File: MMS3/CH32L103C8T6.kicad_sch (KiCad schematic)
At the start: 21 parts, among them J3 WCH Link, U2 CH32L103C8T6_C22398291, X3 X322525MOB4SI, X4 Q13FC1350000400

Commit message: kinda finished schematic
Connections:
- net +3.3V: no longer C30.1, C31.1, C32.1, C33.1, C34.1, R8.2, S1.2 (B), U2.1 (VBAT), U2.24 (VDD), U2.36 (VDD), U2.48 (VDD), U2.9 (VDDA)
- new net +3V3: C30.1, C31.1, C32.1, C33.1, C34.1, R8.2, S1.2 (B), U2.1 (VBAT), U2.24 (VDD), U2.36 (VDD), U2.48 (VDD), U2.9 (VDDA)
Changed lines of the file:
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@@
-	)
-	(symbol
-		(lib_id "power:+3.3V")
-		(at 187.96 120.65 0)
-		(unit 1)
-		(body_style 1)
-		(exclude_from_sim no)
-		(in_bom yes)
-		(on_board yes)
-		(in_pos_files yes)
-		(dnp no)
-		(fields_autoplaced yes)
-		(property "Reference" "#PWR016"
-			(at 187.96 124.46 0)
-			(hide yes)
-			(show_name no)
-			(do_not_autoplace no)
-			(effects
-				(font
-					(size 1.27 1.27)
-				)
-			)
-		)
-		(property "Value" "+3.3V"
-			(at 187.96 115.57 0)
-			(show_name no)
-			(do_not_autoplace no)
-			(effects
-				(font
-					(size 1.27 1.27)
-				)
-			)
-		)
-		(property "Footprint" ""
-			(at 187.96 120.65 0)
-			(hide yes)
-			(show_name no)
-			(do_not_autoplace no)
-			(effects
-				(font
-					(size 1.27 1.27)
-				)
-			)
-		)
-		(property "Datasheet" ""
-			(at 187.96 120.65 0)
-			(hide yes)
-			(show_name no)
-			(do_not_autoplace no)
-			(effects
-				(font
-					(size 1.27 1.27)
-				)
-			)
-		)
-		(property "Description" "Power symbol creates a global label with name \"+3.3V\""
-			(at 187.96 120.65 0)
-			(hide yes)
-			(show_name no)
-			(do_not_autoplace no)
-			(effects
-				(font
-					(size 1.27 1.27)
-				)
-			)
-		)
-		(pin "1"
-		)
-		(instances
-			(project "MMS3"
-				(path "/712cea22-140d-4c92-923f-f4998caf3ecd/ec639d08-3c03-4054-a7c4-c3d480e6d770/8d009271-d3bb-4150-9191-494f39201dbc"
-					(reference "#PWR016")
-					(unit 1)
-				)
-			)
-		)
 	)
 	(symbol
@@
 					(unit 1)
 				)
+			)
+		)
+	)
+	(symbol
+		(lib_id "power:+3V3")
+		(at 187.96 120.65 0)
+		(unit 1)
+		(body_style 1)
+		(exclude_from_sim no)
+		(in_bom yes)
+		(on_board yes)
+		(in_pos_files yes)
+		(dnp no)
+		(fields_autoplaced yes)
+		(property "Reference" "#PWR063"
+			(at 187.96 124.46 0)
+			(hide yes)
+			(show_name no)
+			(do_not_autoplace no)
+			(effects
+				(font
+					(size 1.27 1.27)
+				)
+			)
+		)
+		(property "Value" "+3V3"
+			(at 187.96 115.57 0)
+			(show_name no)
+			(do_not_autoplace no)
+			(effects
+				(font
+					(size 1.27 1.27)
+				)
+			)
+		)
+		(property "Footprint" ""
+			(at 187.96 120.65 0)
+			(hide yes)
+			(show_name no)
+			(do_not_autoplace no)
+			(effects
+				(font
+					(size 1.27 1.27)
+				)
+			)
+		)
+		(property "Datasheet" ""
+			(at 187.96 120.65 0)
+			(hide yes)
+			(show_name no)
+			(do_not_autoplace no)
+			(effects
+				(font
+					(size 1.27 1.27)
+				)
+			)
+		)
+		(property "Description" "Power symbol creates a global label with name \"+3V3\""
+			(at 187.96 120.65 0)
+			(hide yes)
+			(show_name no)
+			(do_not_autoplace no)
+			(effects
+				(font
+					(size 1.27 1.27)
+				)
+			)
+		)
+		(pin "1"
+		)
+		(instances
+			(project "MMS3"
+				(path "/712cea22-140d-4c92-923f-f4998caf3ecd/ec639d08-3c03-4054-a7c4-c3d480e6d770/8d009271-d3bb-4150-9191-494f39201dbc"
+					(reference "#PWR063")
+					(unit 1)
+				)

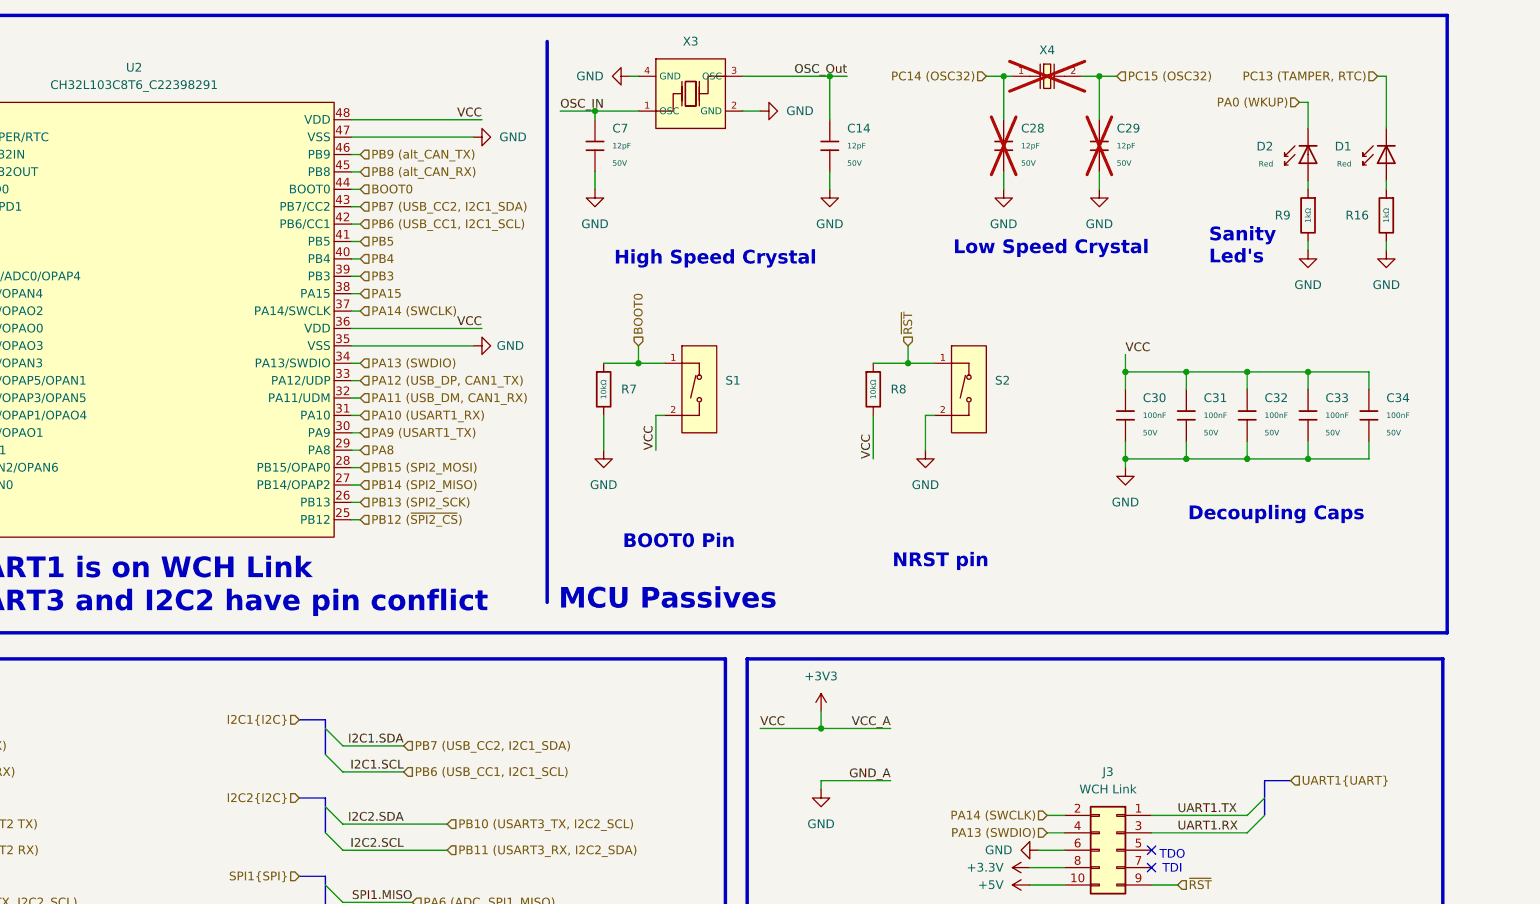
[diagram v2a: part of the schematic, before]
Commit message: updated schematic, removed annotation
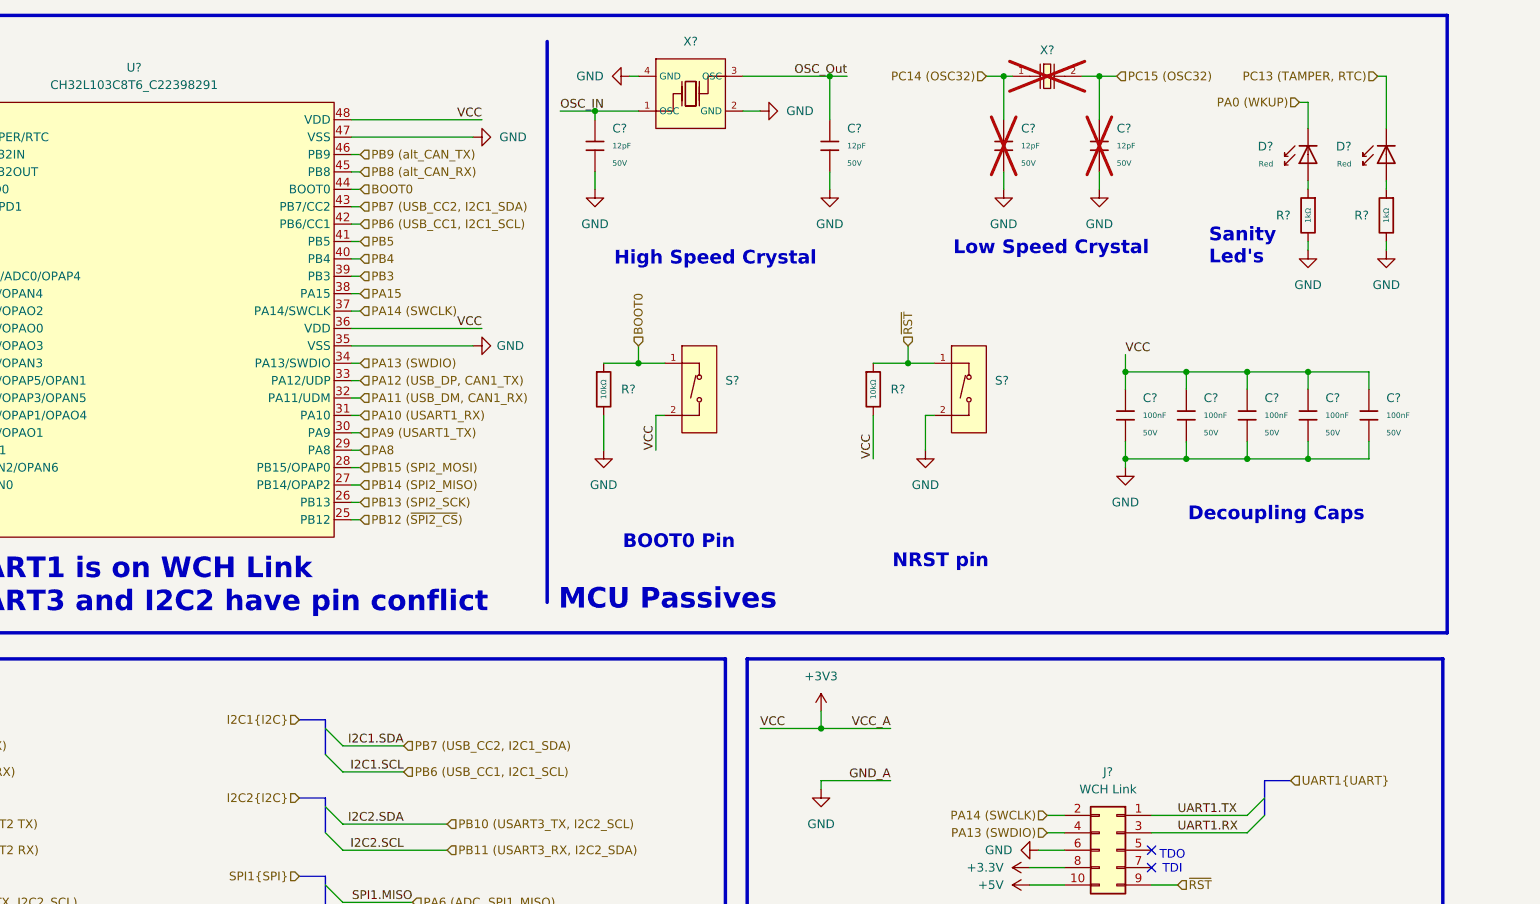
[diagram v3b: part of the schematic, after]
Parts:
- renumbered C32 to C?, C28 to C?, C31 to C?, C30 to C?, C34 to C?, C14 to C?, C29 to C?, C7 to C?, C33 to C?, D1 to D?, D2 to D?, J3 to J?, R7 to R?, R16 to R?, R8 to R?, R9 to R?, S1 to S?, S2 to S?, U2 to U?, X3 to X?, X4 to X?
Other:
- company: (none) -> (c) Modular Mechanica
- title: (none) -> MMS3 CH32L103 Version

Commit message: initial PCB update
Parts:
- gave numbers to parts that had none: 21

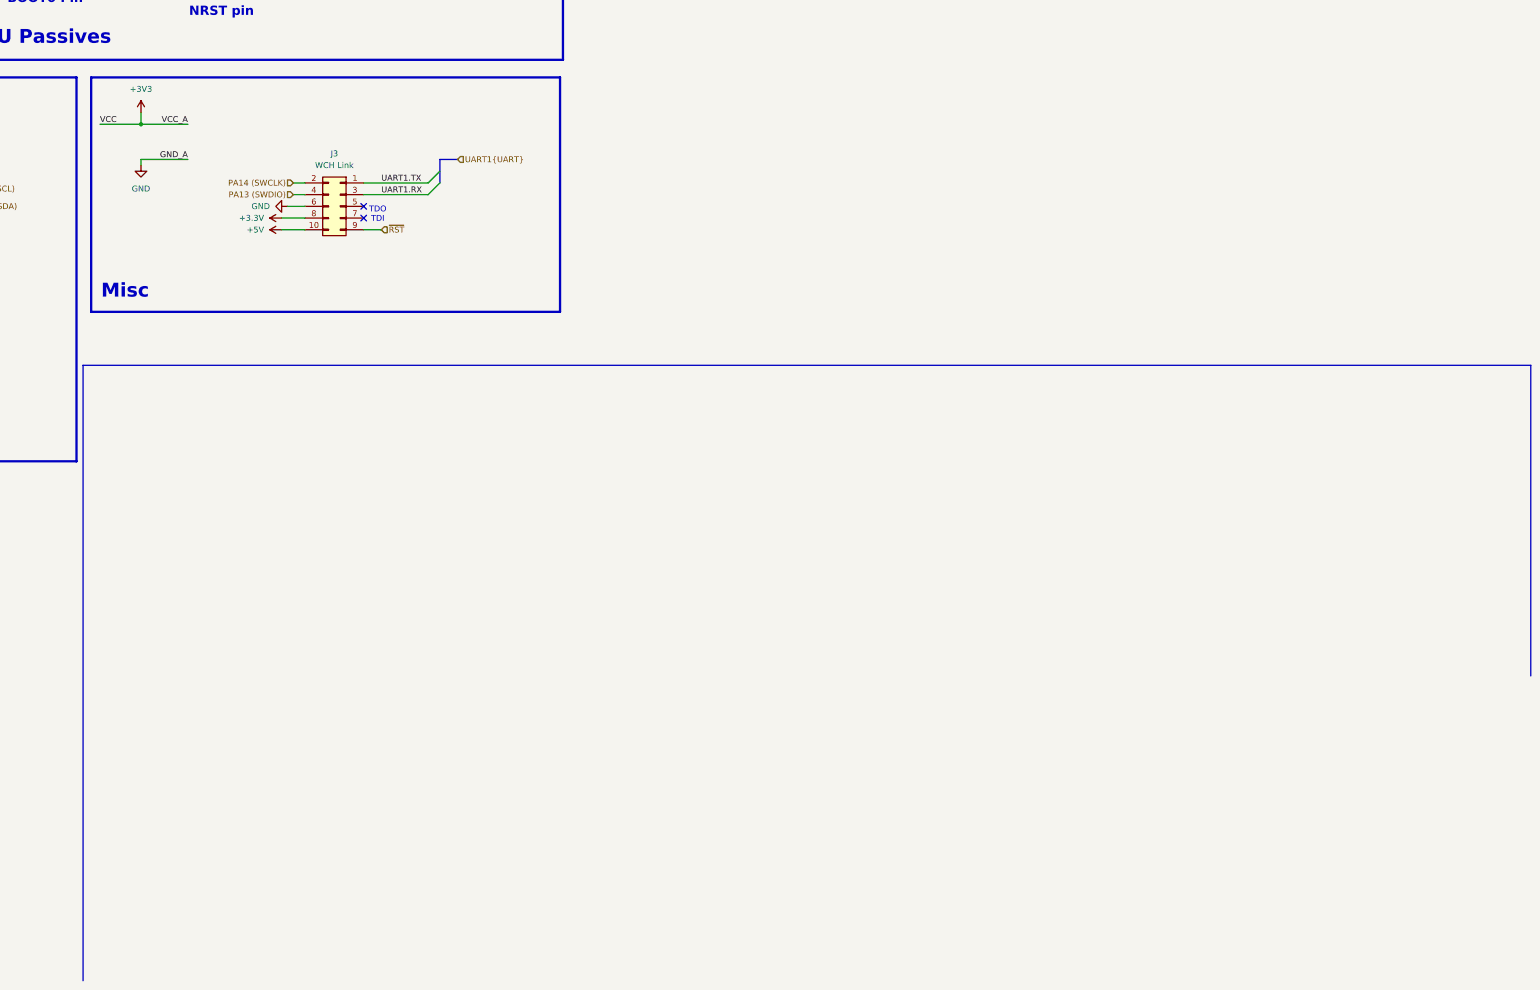
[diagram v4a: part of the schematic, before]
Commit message: re-added onboard programmer
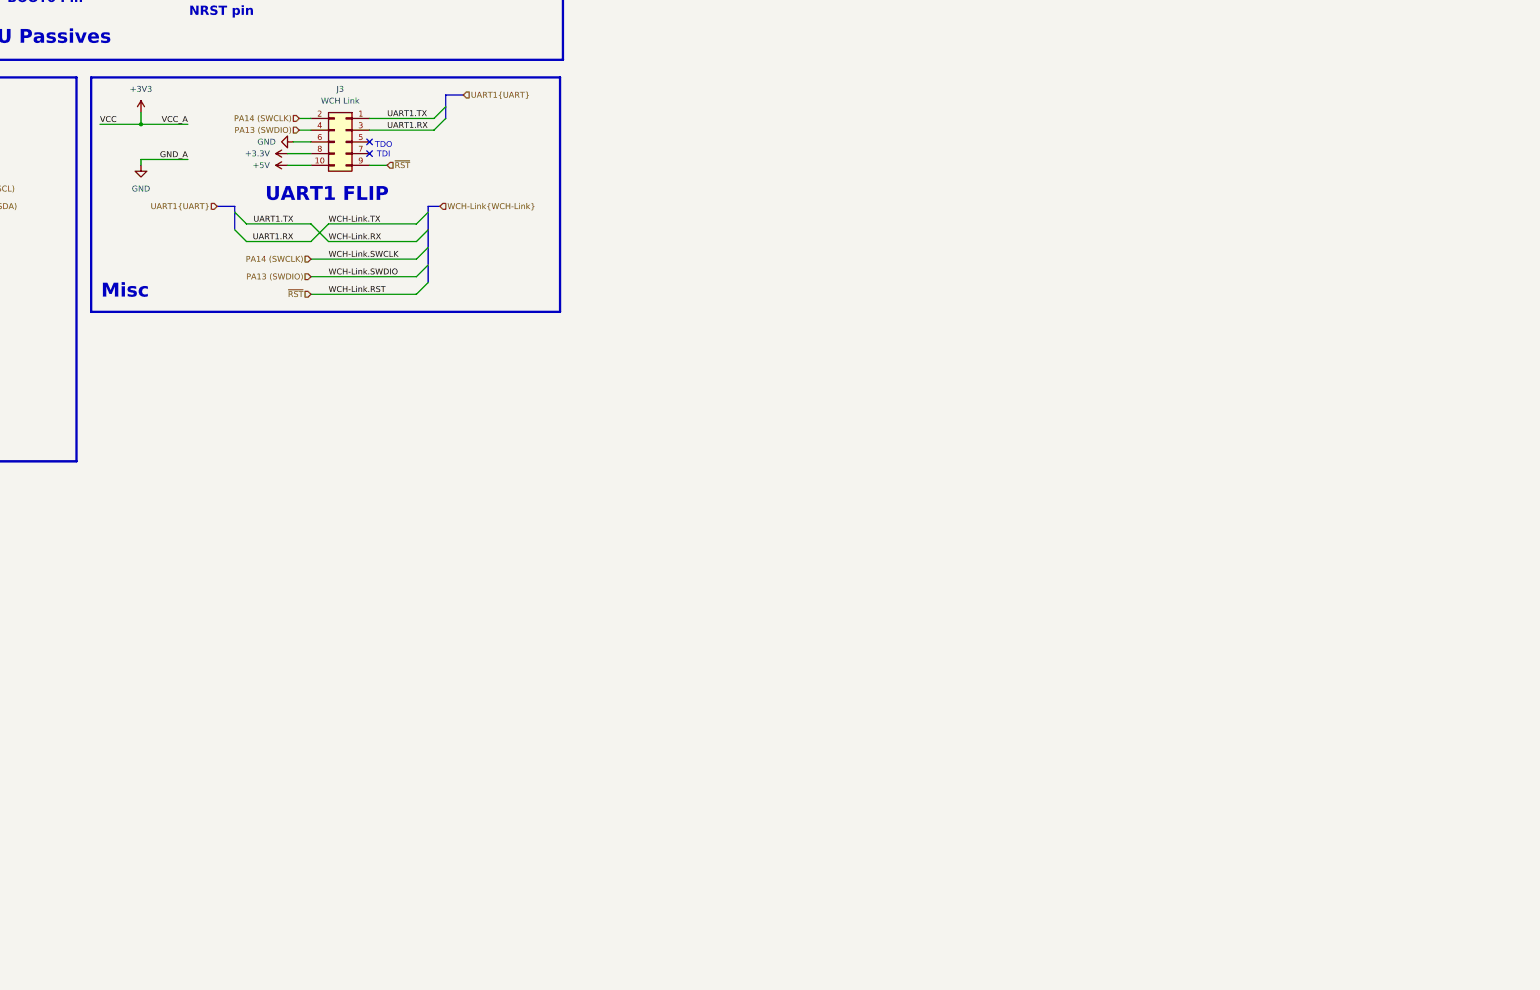
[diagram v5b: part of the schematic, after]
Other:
- note added: "UART1 FLIP"
- moved on the sheet: J3
